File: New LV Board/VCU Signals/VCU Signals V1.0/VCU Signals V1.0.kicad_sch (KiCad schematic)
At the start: 13 parts, among them J1 B12B-PH-K-S:JST_B12B-PH-K-S, U1 IRLML2060TRPBF, U2 IRLML2060TRPBF, U3 IRLML2060TRPBF

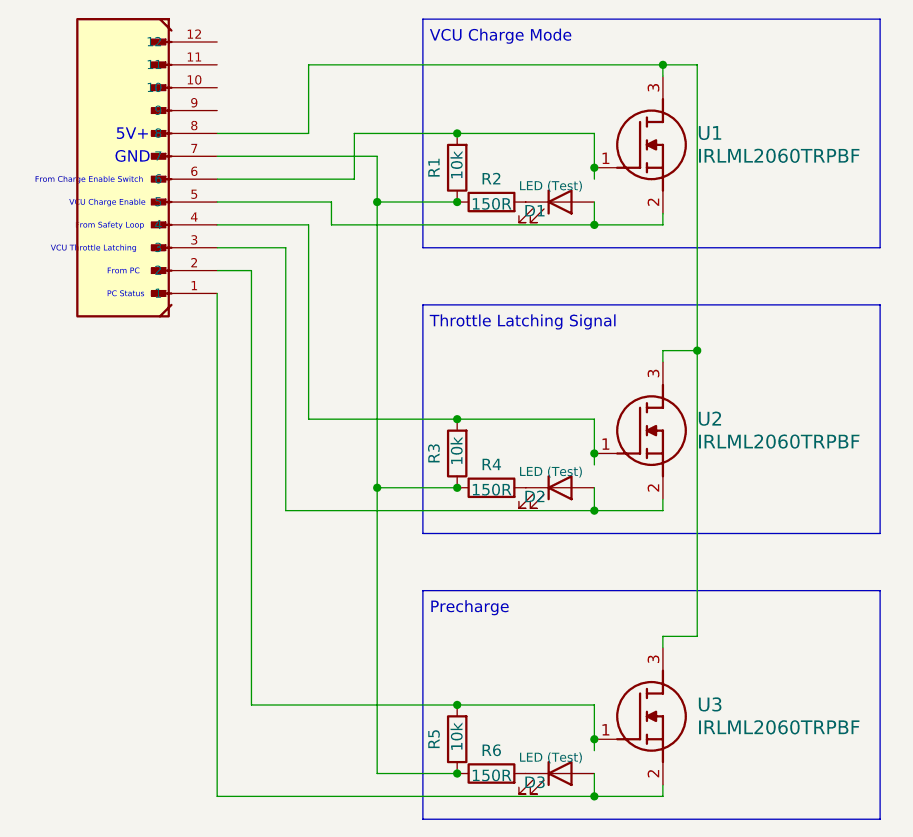
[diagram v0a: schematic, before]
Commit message: updated VCU signals with substitute mosfets
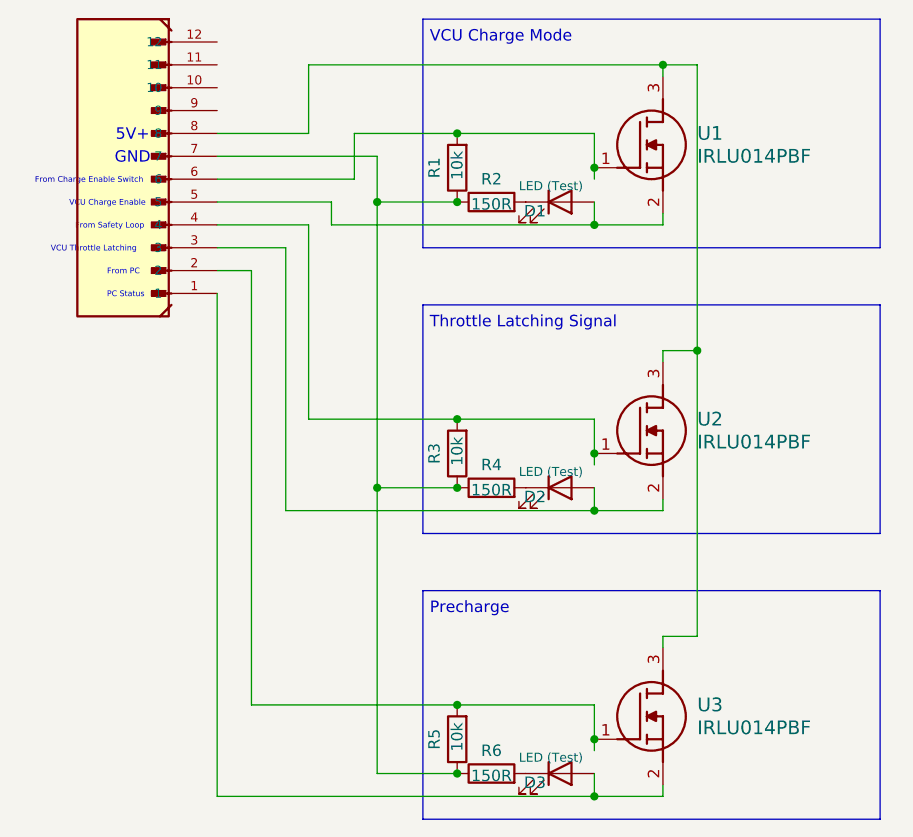
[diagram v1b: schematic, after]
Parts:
- U1, U2, U3: value IRLML2060TRPBF -> IRLU014PBF; footprint Motorsports:DPAK-3_6P35X6P73_ONS -> Package_TO_SOT_THT:TO-251-3_Vertical
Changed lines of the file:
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@@
 			)
 		)
-		(property "Value" "IRLML2060TRPBF"
+		(property "Value" "IRLU014PBF"
 			(at 93.98 40.6399 0)
 			(effects
@@
 			)
 		)
-		(property "Footprint" "Motorsports:DPAK-3_6P35X6P73_ONS"
+		(property "Footprint" "Package_TO_SOT_THT:TO-251-3_Vertical"
 			(at 93.98 140.64 0)
 			(effects
@@
 			)
 		)
-		(property "Datasheet" "https://www.infineon.com/dgdl/irlml2060pbf.pdf?fileId=5546d462533600a401535664b7fb25ee"
+		(property "Datasheet" "https://www.digikey.com/en/products/detail/vishay-siliconix/IRLU014PBF/812390?utm_source=chatgpt.com"
 			(at 93.98 240.64 0)
 			(effects
@@
 			)
 		)
-		(property "Value" "IRLML2060TRPBF"
+		(property "Value" "IRLU014PBF"
 			(at 93.98 104.1399 0)
 			(effects
@@
 			)
 		)
-		(property "Footprint" "Motorsports:DPAK-3_6P35X6P73_ONS"
+		(property "Footprint" "Package_TO_SOT_THT:TO-251-3_Vertical"
 			(at 93.98 204.14 0)
 			(effects
@@
 			)
 		)
-		(property "Datasheet" "https://www.infineon.com/dgdl/irlml2060pbf.pdf?fileId=5546d462533600a401535664b7fb25ee"
+		(property "Datasheet" "https://www.digikey.com/en/products/detail/vishay-siliconix/IRLU014PBF/812390?utm_source=chatgpt.com"
 			(at 93.98 304.14 0)
 			(effects
@@
 			)
 		)
-		(property "Value" "IRLML2060TRPBF"
+		(property "Value" "IRLU014PBF"
 			(at 93.98 72.3899 0)
 			(effects
@@
 			)
 		)
-		(property "Footprint" "Motorsports:DPAK-3_6P35X6P73_ONS"
+		(property "Footprint" "Package_TO_SOT_THT:TO-251-3_Vertical"
 			(at 93.98 172.39 0)
 			(effects
@@
 			)
 		)
-		(property "Datasheet" "https://www.infineon.com/dgdl/irlml2060pbf.pdf?fileId=5546d462533600a401535664b7fb25ee"
+		(property "Datasheet" "https://www.digikey.com/en/products/detail/vishay-siliconix/IRLU014PBF/812390?utm_source=chatgpt.com"
 			(at 93.98 272.39 0)
 			(effects

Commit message: AMS & IMD fixing some connections
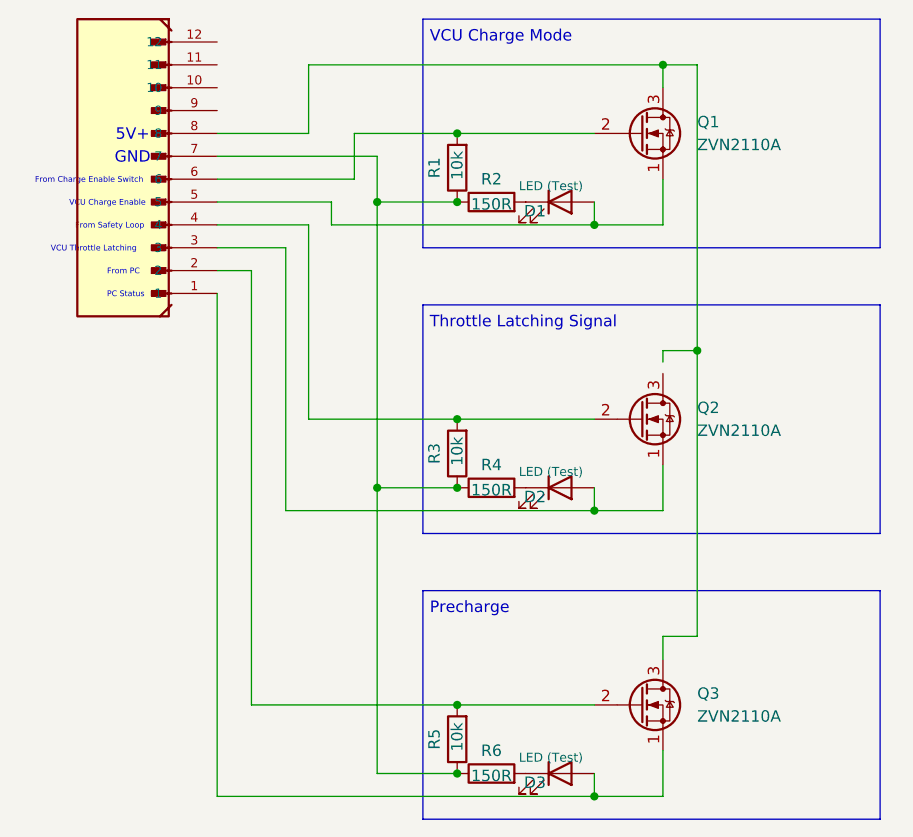
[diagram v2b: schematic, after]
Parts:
- removed U1, U2, U3: IRLU014PBF, Package_TO_SOT_THT:TO-251-3_Vertical, symbol IRLML2060TRPBF:IRLML2060TRPBF
- added Q1, Q2, Q3: ZVN2110A, Package_TO_SOT_THT:TO-92_Inline, symbol Transistor_FET:2N7000
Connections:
- net at J1.6, R1.2: now also Q1.2 (G)
- net at D1.2 (A), J1.5: now also Q1.1 (S)
- net at J1.4, R3.2: now also Q2.2 (G)
- net at J1.2, R5.2: now also Q3.2 (G)
- net at J1.8: now also Q1.3 (D), Q3.3 (D)
- net at D2.2 (A), J1.3: now also Q2.1 (S)
- net at D3.2 (A), J1.1: now also Q3.1 (S)

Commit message: VCU MPR 5V
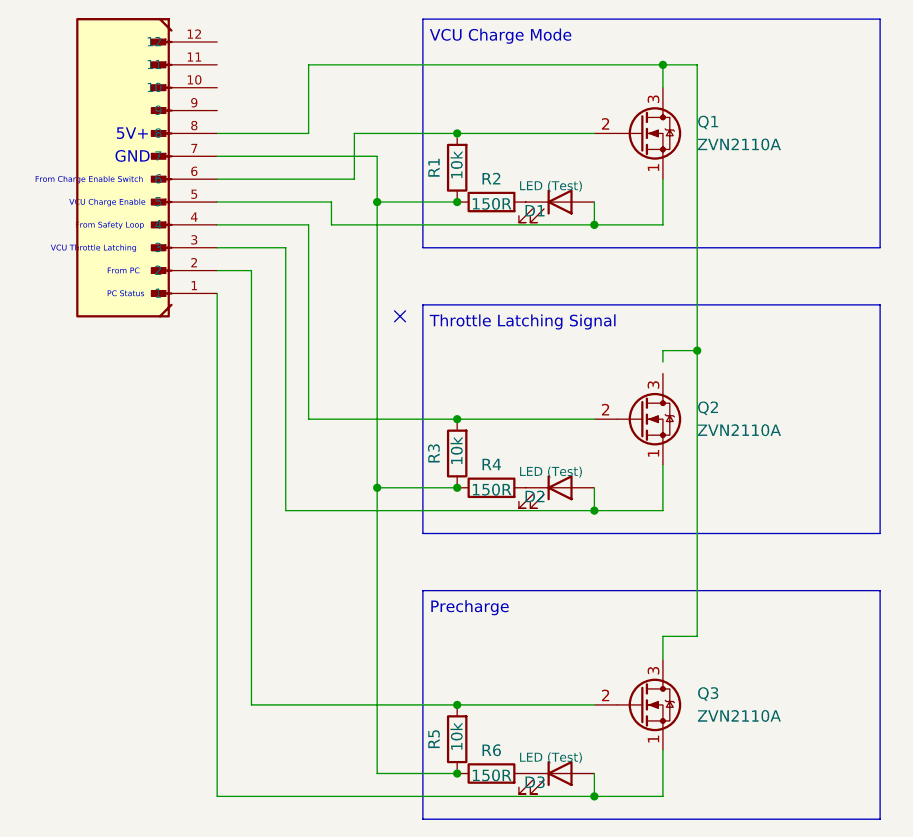
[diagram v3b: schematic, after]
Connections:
- no-connect marks 0 -> 1
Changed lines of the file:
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@@
 		(color 0 0 0 1)
+	)
+	(no_connect
+		(at 60.96 58.42)
 	)
 	(wire
